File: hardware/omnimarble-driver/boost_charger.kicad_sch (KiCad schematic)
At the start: 44 parts, among them K1 HF3FF-12V, K2 HF3FF-12V, Q1 MMBT3904, Q2 MMBT3904, Q3 MMBT3904, Q91 AOD66923, U4 UC3843B, U5 CJ431-0.5%

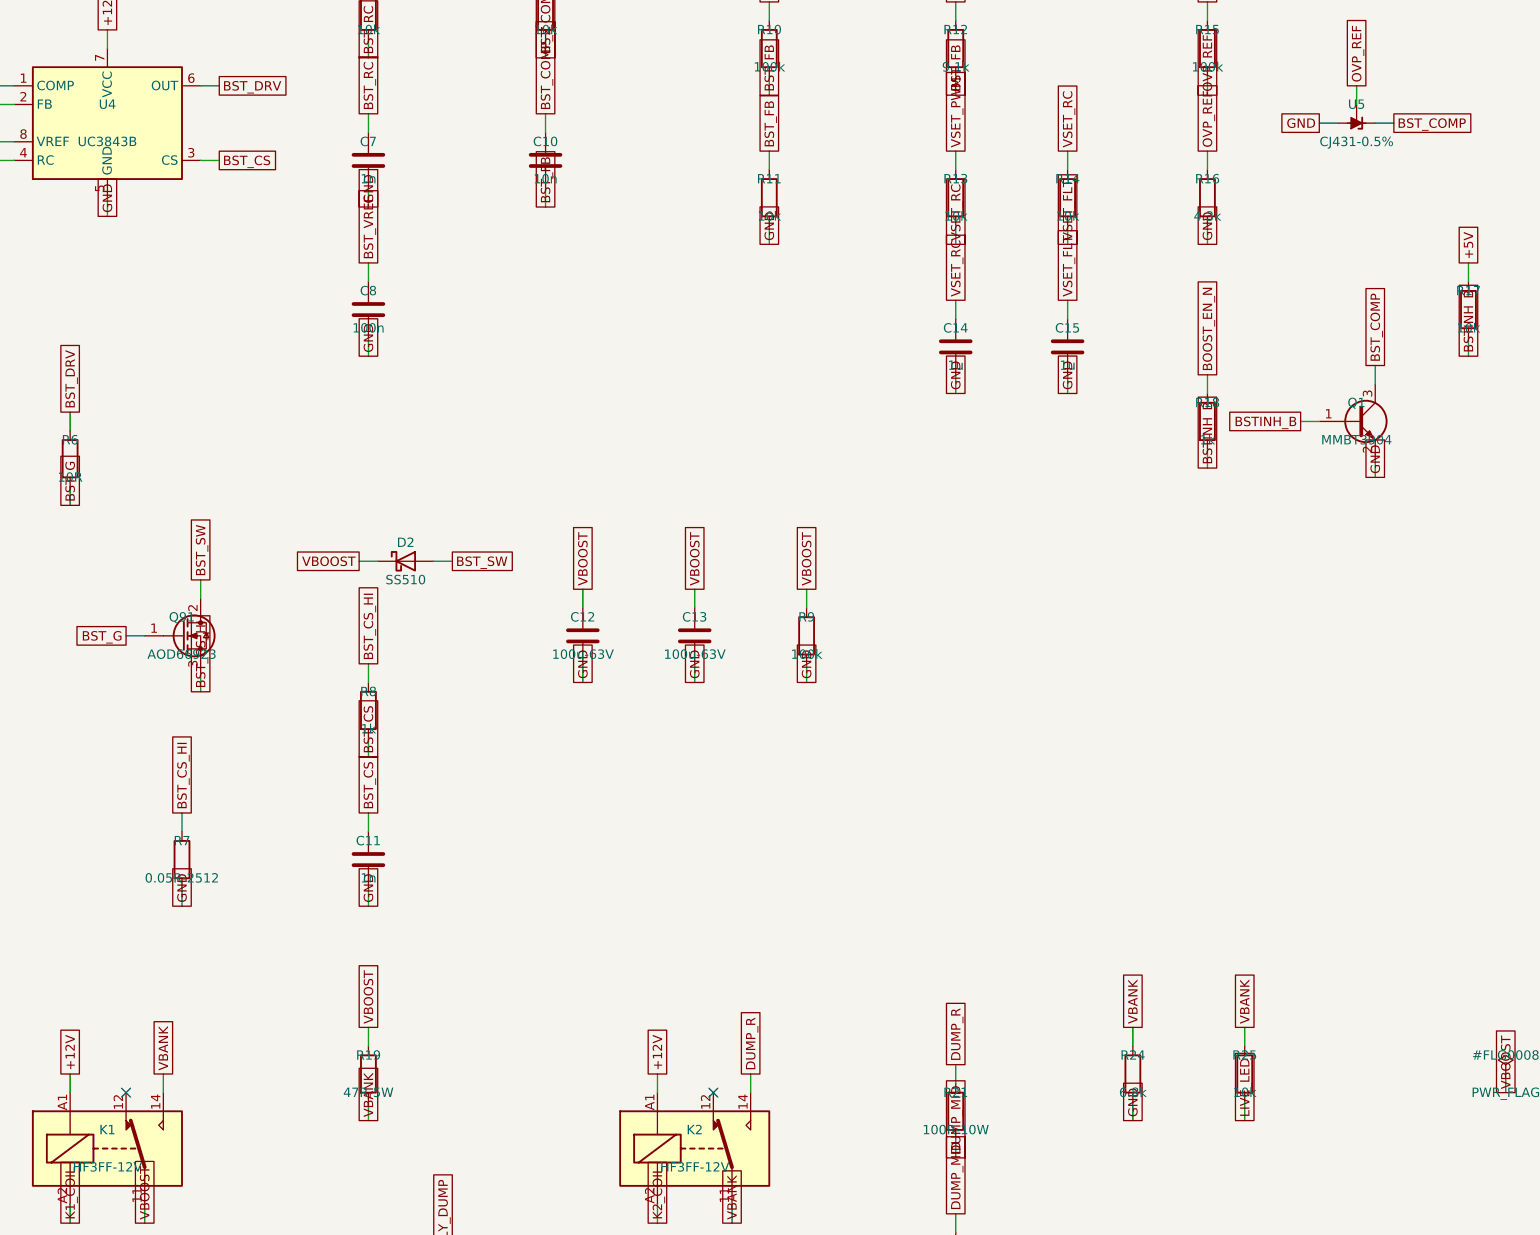
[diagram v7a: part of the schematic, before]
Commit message: Driver PCB: resolve both safety blockers + should-fixes, re-route, DRC-clean
Two datasheet-level blockers (invisible to netlist checks) + the should-fixes
from two review rounds, then a full DeepPCB re-route on the corrected netlist.

Blockers:
- U5 shunt ref: CJ431/C3113 (pinout 1=REF,2=K,3=A) did NOT match the TL431DBZ
  footprint -> OVP dead. Now TL431BIDBZR/C41283 (+/-0.5%, 1=K,2=REF,3=A). Kept
  +/-0.5% grade (the 1% A-grade would blow the 62.0V OVP ceiling).
- Relay HF3FF footprint had NO/NC transposed (datasheet bottom-view copied
  without mirroring) -> dump/charge logic inverted. Swapped pads 12<->14 +
  corrected silk. VERIFY WITH OHMMETER at bring-up (COM-NC @rest) -- parity is
  green by construction, DRC cannot see this.

Should-fixes: D90 SMBJ33A->SMBJ26CA (bidirectional, clamps below AP63205);
snubber 4.7k->4.7Ohm; R7 0.05->0.15Ohm (boost ilim); R25 10k->47k (0.28W->0.06W
LED series); BZ1 polarity swap. 78L12->DPAK deferred (reflows the placement
band; documented, fan-cool for bench per user).

Routing: full DeepPCB re-route from the corrected DSN. dsn_fixup now injects a
B.Cu keepout over the FET-strip corridor so the router can't pack signals where
the SHUNT_HI bus lives (rev-40 dropped the locked bus). import-clean re-authors
the SHUNT_HI B.Cu bus deterministically. Post-import repairs: re-authored the
RS1->NT1 Kelvin tie (DeepPCB routed SHUNT_HI on F.Cu shorting ISNS_P), joined a
MCU_FIRE via gap, bulged GATE6 off a 3V3 via, island-removal + a stitch via to
unify the fragmented F.Cu SHUNT_HI pour.

DRC 0 electrical / 0 unconnected; validate.py --production, validate_widths,
check_netlist, calcs all PASS.

Co-Authored-By: Claude Opus 4.8 <noreply@anthropic.com>
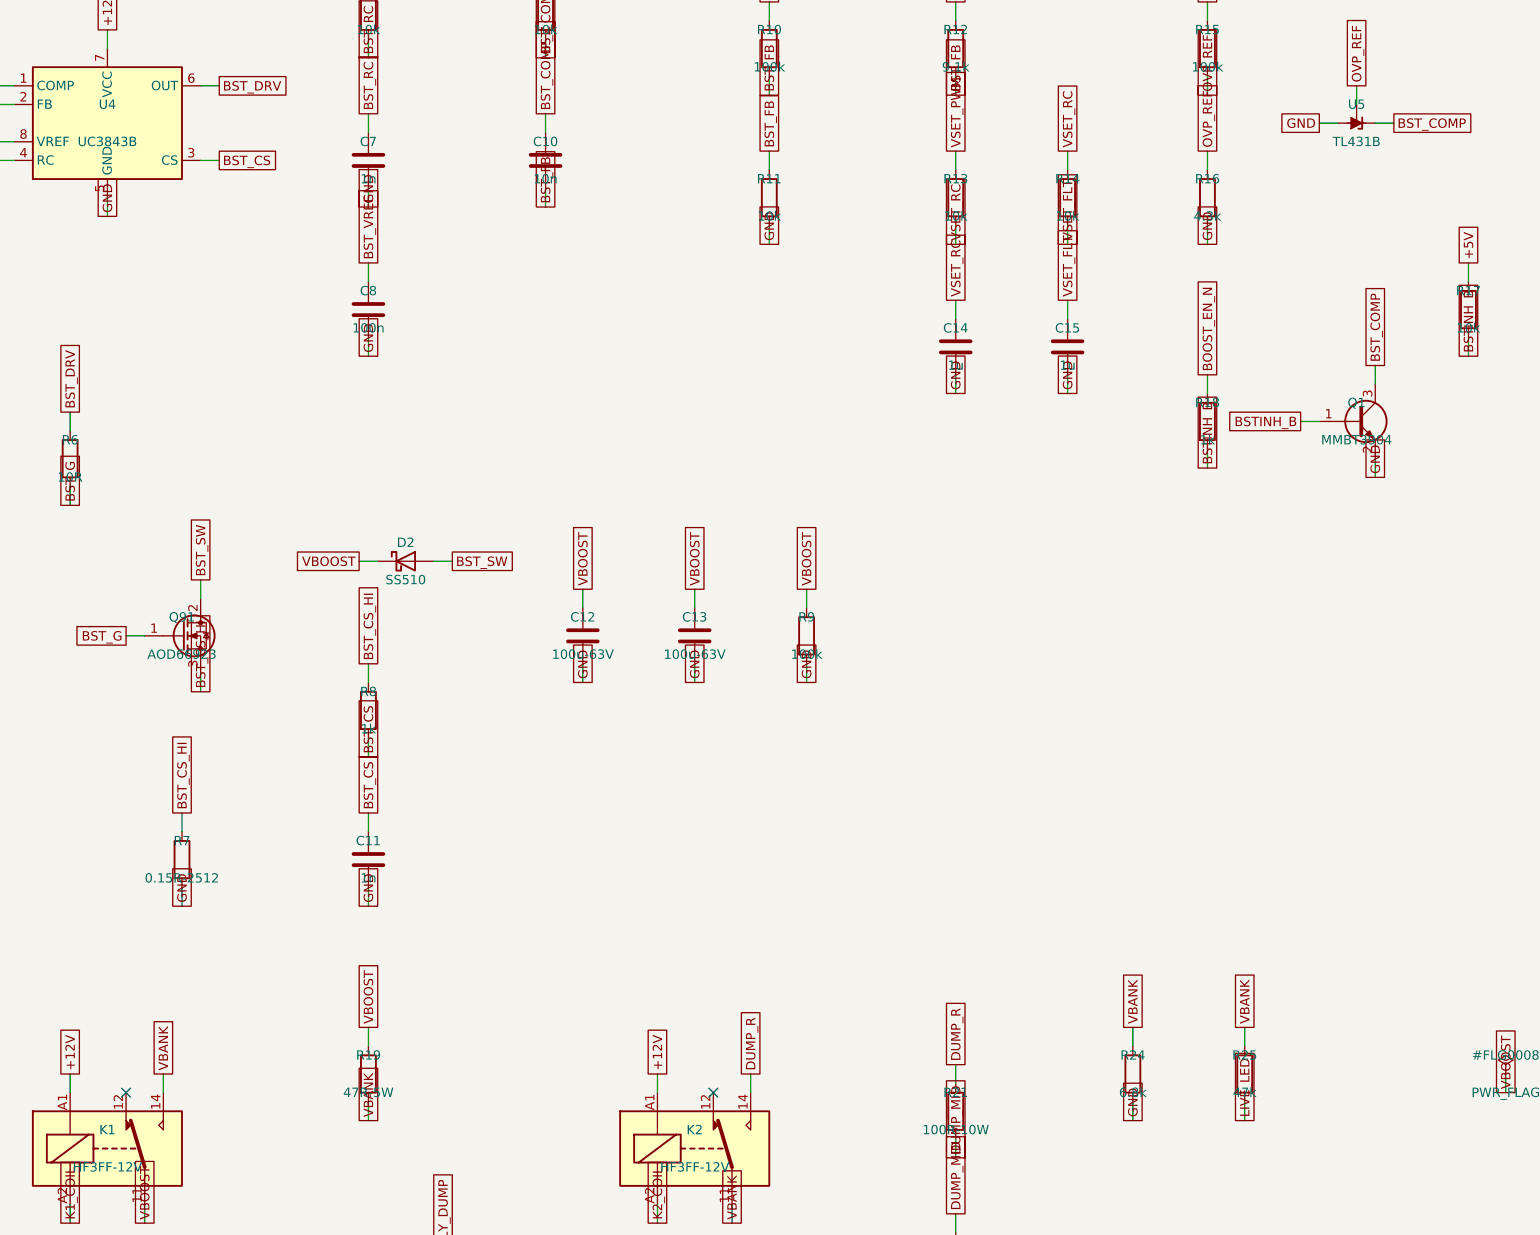
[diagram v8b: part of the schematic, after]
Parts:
- R25: value 10k -> 47k; LCSC C25804 -> C25819
- R7: value 0.05R-2512 -> 0.15R-2512; LCSC C2994645 -> C2903485
- U5: value CJ431-0.5% -> TL431B; LCSC C3113 -> C41283
